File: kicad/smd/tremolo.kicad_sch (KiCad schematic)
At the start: 25 parts, among them IC2 TL072CP

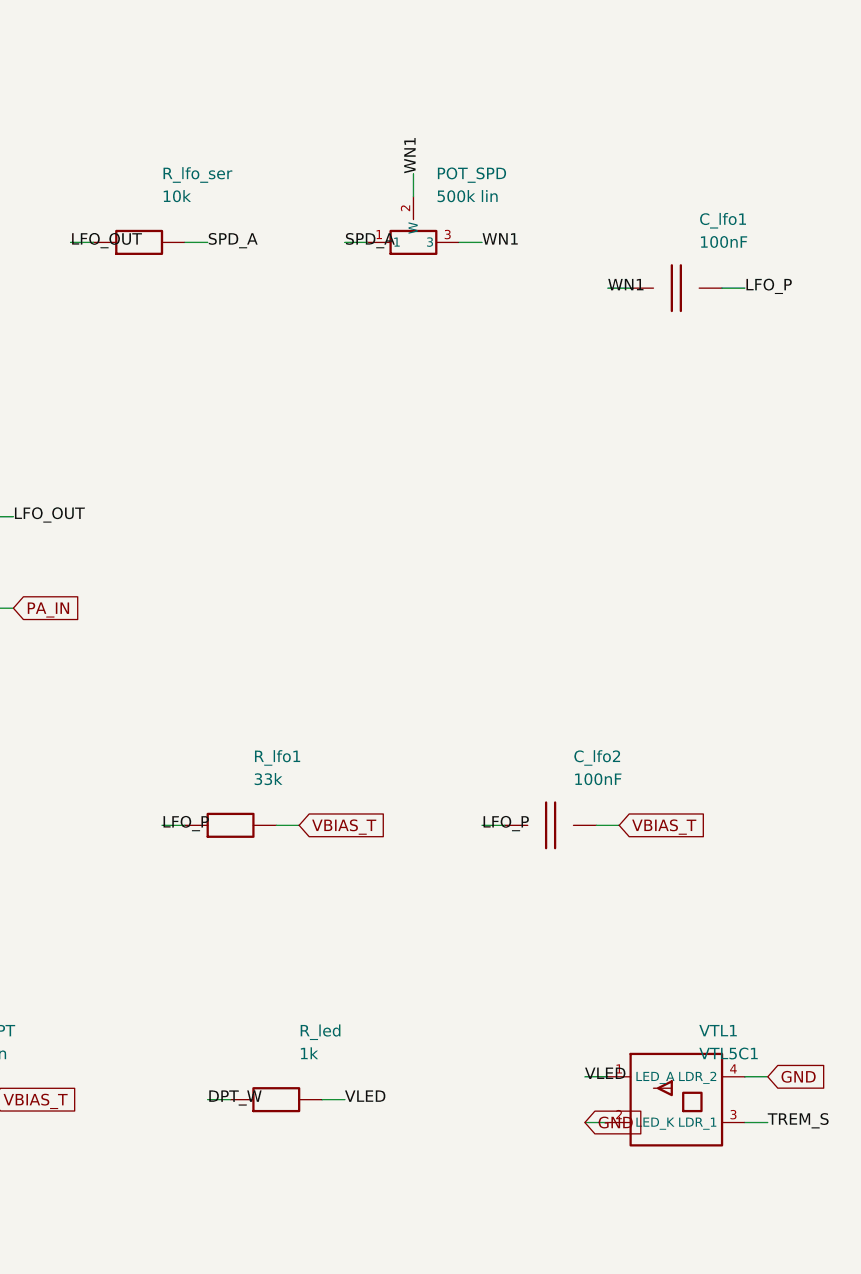
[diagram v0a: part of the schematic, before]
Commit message: SPICE parameter sweeps with committed results; tremolo LFO fix (errata #19); re-route
spice/: six ngspice sweeps next to the fixed-point checks, and run_all.sh now
saves every result table to spice/results/ (committed evidence):
- sweep_preamp_bias: Vd vs R_s for LO/TYP/HI JFET corners (datasheet Idss 1/3/5
  mA). The recovered 2.2k suits a HIGH-Idss part (8.8 V); a typical part wants
  ~1.0k (8.5 V); a 1 mA part cannot reach 8-9 V at any R_s -> errata #15 quantified
- sweep_tonestack: response over the whole pot travel (1 kHz -1.6..-3.3 dB while
  10 kHz falls 14 dB)
- sweep_lfo_speed_recovered: the recovered single-arm Wien LFO oscillates only for
  pot <= ~27k (5 % of travel) at 45-80 Hz, and not at all elsewhere
- sweep_lfo_speed: the fixed network, 10.6 Hz .. 0.60 Hz at constant 0.96 Vpp
- sweep_classa_bias: standing current / heat / THD vs bias (1.4 % -> 0.002 %,
  0.11 -> 0.85 A)
- sweep_pa_headroom: clean power vs rail, mains -10 %..+10 % = 8.9 / 11.7 / 14.8 W

Errata #19 (HIGH): the tremolo LFO did not work as recovered (Wien start condition
gain > 2 + R1/R2 fails with the speed pot in one arm). Built design: dual-gang
250k lin speed pot (one gang per arm, same panel hole), 15k floors, 1 uF timing
caps; POT_SPD_A/B in schematic + BOM = one part. tran_tremolo_lfo.cir aligned
(10.59 Hz at the fast end). Docs: errata, Part 1 s5, Part 2 note, Part 6b, BOM
cross-check, spice README (sweep tables), PCB-NOTES test-point row, README.

Both boards regenerated and re-routed (six settings each; Freerouting is
deterministic per input but placement-sensitive): THT 167/168, 3 starved-thermal
errors (was 166/166 clean); SMD 162/169, DRC clean (was 165/167 + 1 error).
Reports in kicad/reports/, open links listed in PCB-NOTES.

Co-Authored-By: Claude Fable 5.1 <noreply@anthropic.com>
Claude-Session: https://claude.ai/code/session_01Vk8HkvCugxFpQsBPVnNT2H
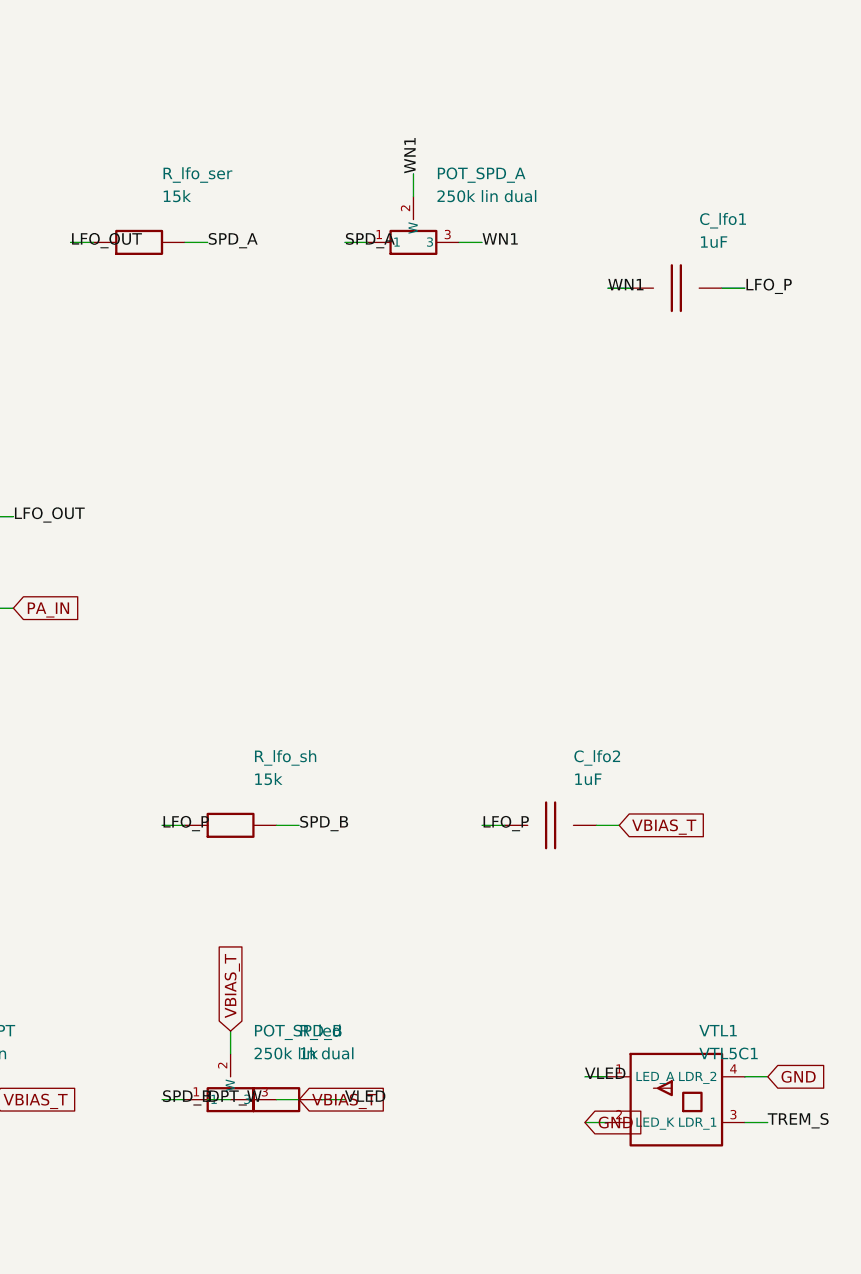
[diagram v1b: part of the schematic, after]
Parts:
- removed POT_SPD: 500k lin, cambridge_reverb:WirePad_1x03_P2.54mm_D1.2mm, symbol cr_primitives:POT
- removed R_lfo1: 33k, Resistor_SMD:R_0805_2012Metric, symbol cr_primitives:R
- added POT_SPD_A, POT_SPD_B: 250k lin dual, cambridge_reverb:WirePad_1x03_P2.54mm_D1.2mm, symbol cr_primitives:POT
- added R_lfo_sh: 15k, Resistor_SMD:R_0805_2012Metric, symbol cr_primitives:R
- C_lfo1, C_lfo2: value 100nF -> 1uF; footprint Capacitor_SMD:C_1206_3216Metric -> Capacitor_SMD:C_1210_3225Metric
- R_lfo_ser: value 10k -> 15k
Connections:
- net LFO_P: now also R_lfo_sh.1
- net SPD_A: now also POT_SPD_A.1
- net VBIAS_T: now also POT_SPD_B.2 (W), POT_SPD_B.3
- net WN1: now also POT_SPD_A.2 (W), POT_SPD_A.3
- new net SPD_B: POT_SPD_B.1, R_lfo_sh.2

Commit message: Noise, hum, crosstalk and thermal models; three design fixes; JLCPCB rules and cost
New models (docs/06c, spice/): a .noise run of the whole front end including the
LM317's own rail noise, the rail-ripple paths to the speaker, a vactrol-level tremolo
depth model, an electro-thermal LM1875 ladder, and a geometric crosstalk audit of the
routed boards (kicad/gen/crosstalk_audit.py). They found three defects:

- Errata #21 (hum + hiss): the LM1875 bias divider had no bypass (+4 dB ripple to
  speaker, 0.4 Vrms of 100 Hz at idle) and the LM317's 0.5 mV of noise reached the
  0 dB-PSRR JFET stages (23 dB above their floor, SNR 34 dB). Fixed with C_bref +
  R_bias3 on the power amp, C_adj on the regulator, and an RC-decoupled +17V_PRE rail
  for Q1/Q2/Q_rec: hum 408 mV -> 0.3 mV, EIN 37 -> 2.7 uV, SNR 34 -> 57 dB.
- Errata #22 (tremolo depth 1.7 dB): the vactrol LED was returned to ground from a
  mid-rail LFO -> 7 mA DC, a fixed -20 dB pad. LED limiter (2 V swing, LED_rate is one
  limiter LED) + Q_trem 2N3904/MMBT3904 emitter follower AC-coupled from the depth
  pot -> 15 dB depth, 0.8 dB insertion loss.
- Errata #23 (fab): stock TO-92 and the LM1875 footprint were under JLCPCB's 0.18 mm
  annular-ring minimum -> TO-92_Inline_Wide and 1.5 mm LM1875 pads; both .kicad_pro
  carry JLC's 2-layer limits as DRC constraints. Cost: all SMD caps 1206 (basic
  library), "(opt)" MRB caps DNP, gyrator on E24 values (same 1.86 H): 7 -> 2
  extended part types, ~$32 -> ~$17 assembly for five boards (kicad/gen/jlc_cost.py);
  three fiducials on the SMD board.

Crosstalk -> two routing rules (.kicad_dru: HighCurrent 0.6/0.4 mm and TankDrive
1.2/0.8 mm from signal copper, THT/SMD) that route_board.py also hands the router as
class clearances; keepout rule areas along the edge and around the mounting holes.
Thermal: Part 5's <= 2.5 K/W heatsink confirmed with numbers (Tj 97 C at 40 C ambient,
worst-case sine; 8-10 K/W clip-ons reach shutdown).

Placer: short parts stack beside tall ones i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
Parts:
- removed D_lfo1, D_lfo2: 1N4148, Diode_SMD:D_SOD-123, symbol cr_primitives:D
- removed R_led: 1k, Resistor_SMD:R_0805_2012Metric, symbol cr_primitives:R
- removed R_led_diag: 2.2k, Resistor_SMD:R_0805_2012Metric, symbol cr_primitives:R
- added C_drv: 100uF/25V, Capacitor_THT:CP_Radial_D6.3mm_P2.50mm, symbol cr_primitives:CP
- added LED_lim: 3mm red, LED_THT:LED_D3.0mm, symbol cr_primitives:LED
- added Q_trem: 2N3904, cambridge_reverb:SOT-23_MMBT3904_as_EBC, symbol cr_primitives:NPN
- added R_b1: 180k, Resistor_SMD:R_0805_2012Metric, symbol cr_primitives:R
- added R_b2: 10k, Resistor_SMD:R_0805_2012Metric, symbol cr_primitives:R
- added R_c: 100R, Resistor_SMD:R_0805_2012Metric, symbol cr_primitives:R
- added R_e: 470R, Resistor_SMD:R_0805_2012Metric, symbol cr_primitives:R
- C_lfo1, C_lfo2, C_obuf_in: footprint Capacitor_SMD:C_1210_3225Metric -> Capacitor_SMD:C_1206_3216Metric
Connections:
- net DLED is gone; now on net LFO_OUT: LED_rate.1 (A)
- net +17V: now also R_b1.1, R_c.1
- net DPT_W: now also C_drv.1 (+)
- net GND: now also R_b2.2, R_e.2; no longer LED_rate.2 (K), VTL1.2 (LED_K)
- net LFO_N: now also LED_rate.2 (K), LED_lim.1 (A)
- net LFO_OUT: now also LED_lim.2 (K)
- net VLED: now also R_c.2
- new net QB: C_drv.2, Q_trem.2 (B), R_b1.2, R_b2.1
- new net QC: Q_trem.3 (C), VTL1.2 (LED_K)
- new net QE: Q_trem.1 (E), R_e.1
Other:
- note added: "TREMOLO -- IC2-A: Wien LFO (0.6-10.6 Hz), limited by two antiparallel LEDs (~2 V swing; LED_rate blinks). Q_trem: AC-coupled emitter follower drives the VTL5C1 LED 0..6 mA -> 15 dB depth, 0.8 dB insertion loss (was 7 mA DC: -20 dB pad, 1.7 dB depth). IC2-B: post-MRB output buffer -> PA_IN."
- note removed: "TREMOLO -- IC2-A: Wien LFO (~16Hz) -> VTL5C1. IC2-B: post-MRB output buffer -> PA_IN. All on VBIAS_T."
